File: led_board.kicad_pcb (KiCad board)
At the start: 2 copper layers, 12 parts, among them J1 Conn_Coaxial, J2 Conn_Coaxial, J3 Conn_Coaxial, J4 Conn_Coaxial

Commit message: edits
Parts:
- moved D4 124.5 mm to (52.5, 109.7), turned to 270 degrees
- moved R4 121.5 mm to (49.2, 109.7)
- moved R3 114.5 mm to (49.0, 87.4)
- moved J4 112.4 mm to (40.4, 109.7), turned to 180 degrees
- moved D3 6.88 mm to (53.2, 88.8), turned to 0 degrees
- moved D2 0.76 mm to (53.0, 65.0)
- moved J2 0.76 mm to (40.4, 65.0)
- moved R2 0.76 mm to (47.6, 65.0)
- moved J3 0.72 mm to (40.4, 87.4)
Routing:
- net Net-(D3-Pad2): track 0.00 -> 29.8 mm
- net Net-(D4-Pad2): track 0.00 -> 29.8 mm
- net Net-(J4-Pad1): track 0.00 -> 7.90 mm
- net Net-(J3-Pad1): track 0.00 -> 7.77 mm
- net Net-(D3-Pad1): track 0.00 -> 3.00 mm
- net Net-(D4-Pad1): track 0.00 -> 2.86 mm

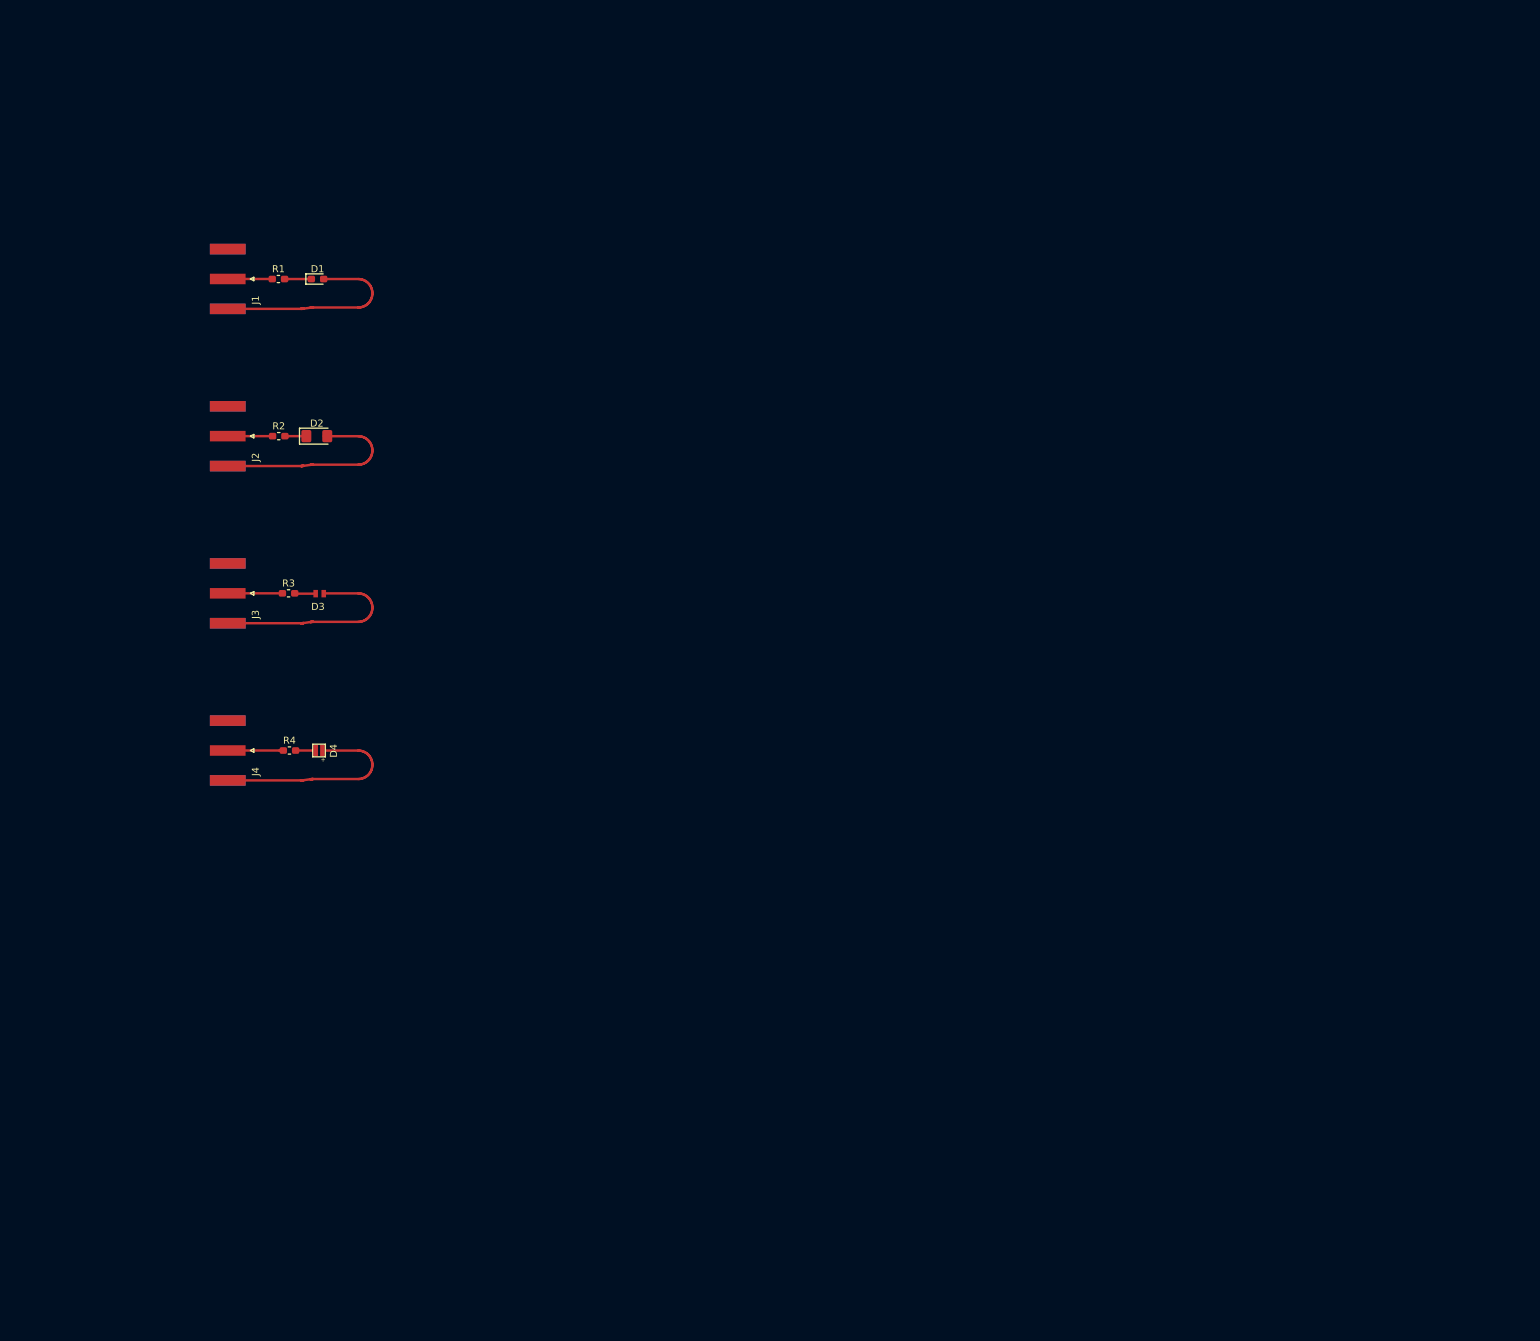
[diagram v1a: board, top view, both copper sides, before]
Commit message: rework for thorlabs 30mm cage
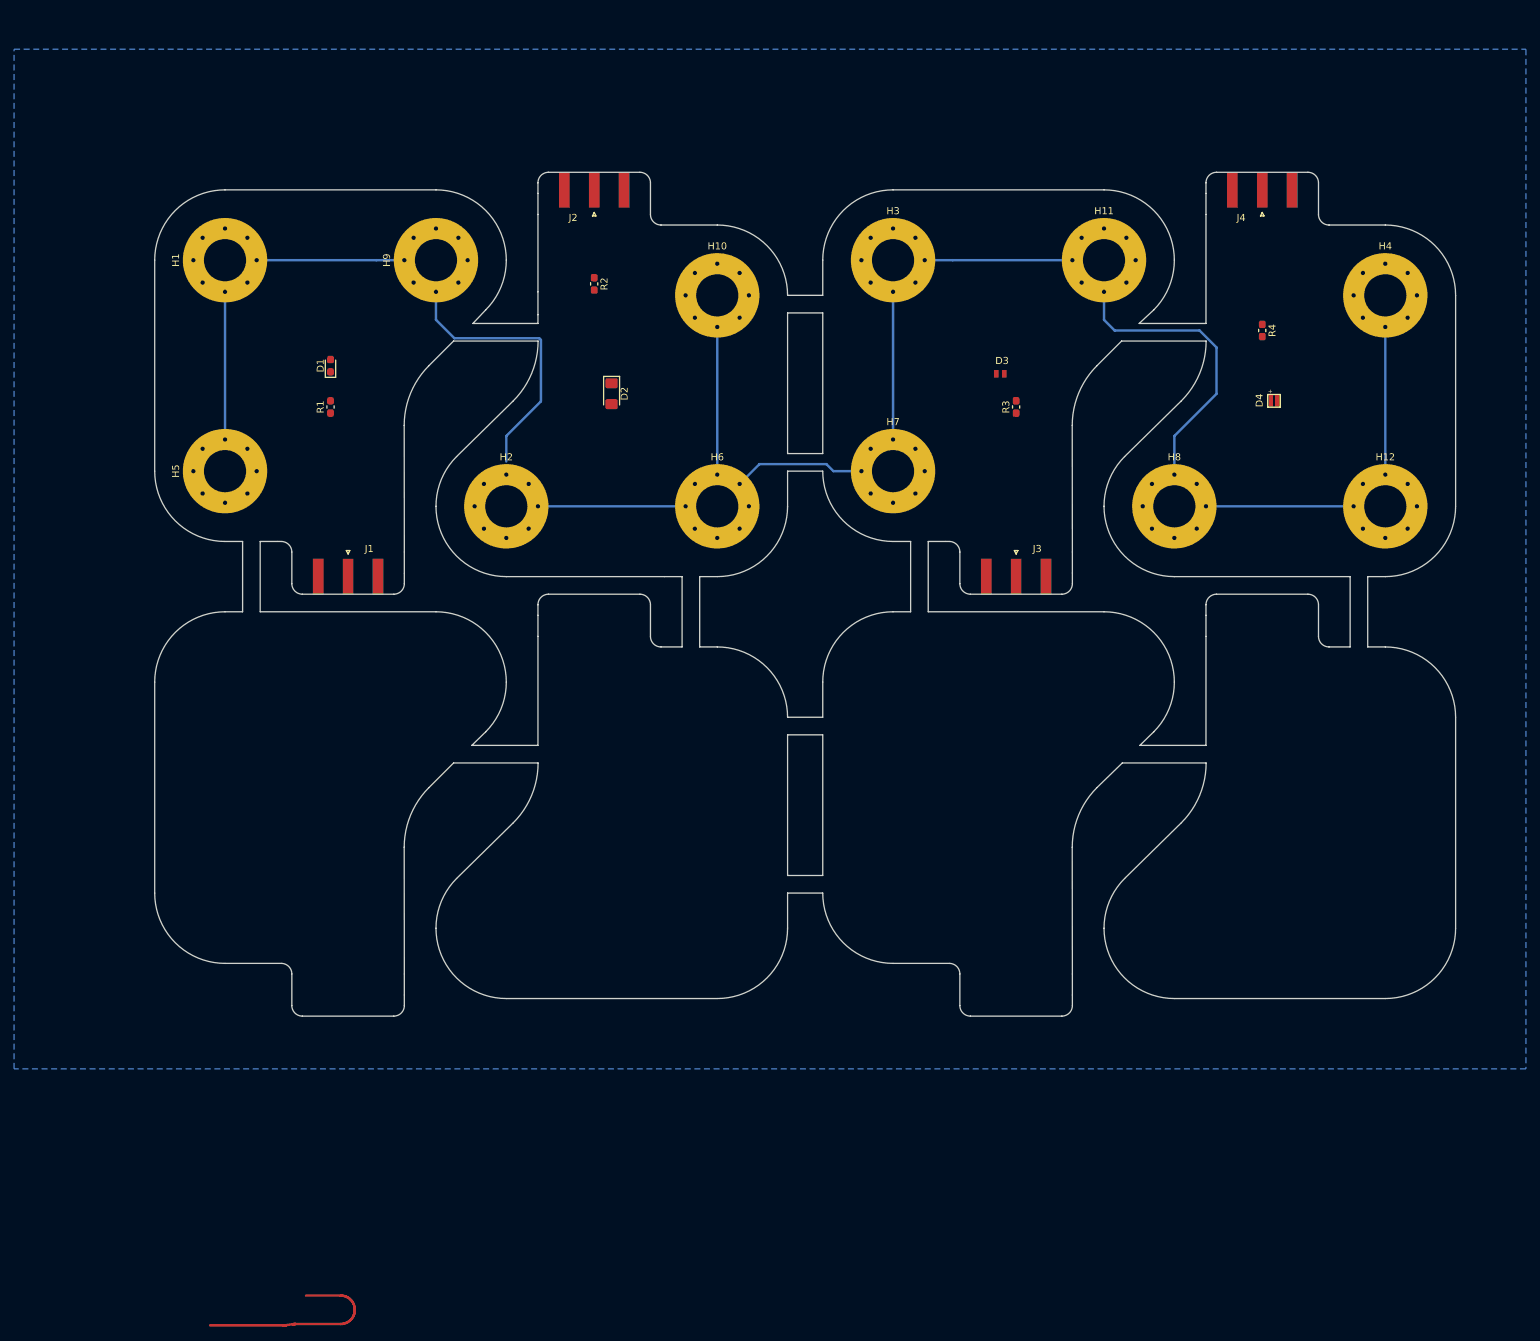
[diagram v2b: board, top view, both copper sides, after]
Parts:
- added H1: MountingHole_Pad, MountingHole:MountingHole_6mm_Pad_Via, F.Cu at (40.0, 40.0)
- added H10: MountingHole_Pad, MountingHole:MountingHole_6mm_Pad_Via, F.Cu at (110.0, 45.0)
- added H11: MountingHole_Pad, MountingHole:MountingHole_6mm_Pad_Via, F.Cu at (165.0, 40.0)
- added H12: MountingHole_Pad, MountingHole:MountingHole_6mm_Pad_Via, F.Cu at (205.0, 75.0)
- added H2: MountingHole_Pad, MountingHole:MountingHole_6mm_Pad_Via, F.Cu at (80.0, 75.0)
- added H3: MountingHole_Pad, MountingHole:MountingHole_6mm_Pad_Via, F.Cu at (135.0, 40.0)
- added H4: MountingHole_Pad, MountingHole:MountingHole_6mm_Pad_Via, F.Cu at (205.0, 45.0)
- added H5: MountingHole_Pad, MountingHole:MountingHole_6mm_Pad_Via, F.Cu at (40.0, 70.0)
- added H6: MountingHole_Pad, MountingHole:MountingHole_6mm_Pad_Via, F.Cu at (110.0, 75.0)
- added H7: MountingHole_Pad, MountingHole:MountingHole_6mm_Pad_Via, F.Cu at (135.0, 70.0)
- added H8: MountingHole_Pad, MountingHole:MountingHole_6mm_Pad_Via, F.Cu at (175.0, 75.0)
- added H9: MountingHole_Pad, MountingHole:MountingHole_6mm_Pad_Via, F.Cu at (70.0, 40.0)
- moved J4 167.3 mm to (187.5, 30.0), turned to 90 degrees
- moved R4 150.7 mm to (187.5, 50.0), turned to 270 degrees
- moved D4 146.2 mm to (190.0, 60.0), turned to 90 degrees
- moved J3 112.1 mm to (152.5, 85.0), turned to 270 degrees
- moved R3 106.8 mm to (152.5, 60.9), turned to 90 degrees
- moved D3 103.0 mm to (150.5, 54.8), turned to 180 degrees
- moved J2 62.8 mm to (92.5, 30.0), turned to 90 degrees
- moved R2 49.8 mm to (92.5, 43.4), turned to 270 degrees
- moved J1 45.7 mm to (57.5, 85.0), turned to 270 degrees
- moved D2 42.4 mm to (95.0, 59.0), turned to 270 degrees
- moved R1 19.6 mm to (55.0, 60.9), turned to 90 degrees
- moved D1 12.5 mm to (55.0, 55.0), turned to 90 degrees
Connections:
- D1 pad 1: Net-(D1-Pad1) -> (no net)
- D1 pad 2: Net-(D1-Pad2) -> (no net)
- J1 pad 1: Net-(J1-Pad1) -> (no net)
- J1 pad 2: Net-(D1-Pad2) -> (no net)
- R1 pad 1: Net-(J1-Pad1) -> (no net)
- R1 pad 2: Net-(D1-Pad1) -> (no net)
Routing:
- net GND: track 0.00 -> 363.0 mm
- net Net-(D1-Pad2): track 29.8 -> 0.00 mm
- net Net-(D3-Pad2): track 29.8 -> 0.00 mm
- net Net-(D2-Pad2): track 29.8 -> 0.00 mm
- net Net-(J4-Pad1): track 7.90 -> 0.00 mm
- net Net-(J3-Pad1): track 7.77 -> 0.00 mm
- net Net-(J1-Pad1): track 6.32 -> 0.00 mm
- net Net-(J2-Pad1): track 6.32 -> 0.00 mm
- net Net-(D1-Pad1): track 3.81 -> 0.00 mm
- net Net-(D2-Pad1): track 3.57 -> 0.00 mm
- net Net-(D3-Pad1): track 3.00 -> 0.00 mm
- net Net-(D4-Pad1): track 2.86 -> 0.00 mm
- added copper zone on B.Cu, net GND
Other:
- board outline added: 185 x 120 mm
- board text added: "£135 for board 2 layer PTH FR4 1oz Cu Au/Ni 0.8mm"

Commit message: fcu pour
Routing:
- added copper zone on F.Cu, net GND
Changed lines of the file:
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@@
   )
   (setup
-    (last_trace_width 0.349)
+    (last_trace_width 0.25)
     (user_trace_width 0.349)
     (trace_clearance 0.2)
@@
   (gr_line (start 65.479186 63.5) (end 65.5 81.5) (layer Edge.Cuts) (width 0.05))
   (gr_arc (start 48 81.5) (end 49.5 81.5) (angle -90) (layer Edge.Cuts) (width 0.05))
-  (segment (start 61.514719 40) (end 40 40) (width 0.349) (layer B.Cu) (net 10))
-  (segment (start 70 40) (end 61.514719 40) (width 0.349) (layer B.Cu) (net 10))
-  (segment (start 40 40) (end 40 70) (width 0.349) (layer B.Cu) (net 10))
-  (segment (start 84.921817 51.333897) (end 84.921817 60.078183) (width 0.349) (layer B.Cu) (net 10))
-  (segment (start 84.68841 51.10049) (end 84.921817 51.333897) (width 0.349) (layer B.Cu) (net 10))
-  (segment (start 72.615209 51.10049) (end 84.68841 51.10049) (width 0.349) (layer B.Cu) (net 10))
-  (segment (start 70 40) (end 70 48.485281) (width 0.349) (layer B.Cu) (net 10))
-  (segment (start 70 48.485281) (end 72.615209 51.10049) (width 0.349) (layer B.Cu) (net 10))
-  (segment (start 84.921817 60.078183) (end 80 65) (width 0.349) (layer B.Cu) (net 10))
-  (segment (start 80 65) (end 80 68.625499) (width 0.349) (layer B.Cu) (net 10))
   (segment (start 48.584912 191.461938) (end 48.609713 191.459153) (width 0.349) (layer F.Cu) (net 5))
   (segment (start 48.609713 191.459153) (end 48.634488 191.456146) (width 0.349) (layer F.Cu) (net 5))
@@
   (segment (start 57.217366 191.131759) (end 57.394793 191.047842) (width 0.349) (layer F.Cu) (net 5))
   (segment (start 58.41357 189.67418) (end 58.442369 189.480034) (width 0.349) (layer F.Cu) (net 5))
+  (segment (start 61.514719 40) (end 40 40) (width 0.349) (layer B.Cu) (net 10))
+  (segment (start 70 40) (end 61.514719 40) (width 0.349) (layer B.Cu) (net 10))
+  (segment (start 40 40) (end 40 70) (width 0.349) (layer B.Cu) (net 10))
+  (segment (start 84.921817 51.333897) (end 84.921817 60.078183) (width 0.349) (layer B.Cu) (net 10))
+  (segment (start 84.68841 51.10049) (end 84.921817 51.333897) (width 0.349) (layer B.Cu) (net 10))
+  (segment (start 72.615209 51.10049) (end 84.68841 51.10049) (width 0.349) (layer B.Cu) (net 10))
+  (segment (start 70 40) (end 70 48.485281) (width 0.349) (layer B.Cu) (net 10))
+  (segment (start 70 48.485281) (end 72.615209 51.10049) (width 0.349) (layer B.Cu) (net 10))
+  (segment (start 84.921817 60.078183) (end 80 65) (width 0.349) (layer B.Cu) (net 10))
+  (segment (start 80 65) (end 80 68.625499) (width 0.349) (layer B.Cu) (net 10))
   (segment (start 80 75) (end 110 75) (width 0.349) (layer B.Cu) (net 10))
   (segment (start 110 75) (end 110 45) (width 0.349) (layer B.Cu) (net 10))
@@
       )
     )
+  )
+  (zone (net 10) (net_name GND) (layer F.Cu) (hatch edge 0.508)
+    (connect_pads (clearance 0.508))
+    (min_thickness 0.254)
+    (fill yes (arc_segments 32) (thermal_gap 0.508) (thermal_bridge_width 0.508))
+    (polygon
+      (pts
+        (xy 225 155) (xy 14 155) (xy 14 5) (xy 225 5)
+      )
+    )

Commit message: no res term boards added, net class updated
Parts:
- added D5: 405LED1, LED_SMD:LED_0603_1608Metric_Pad1.05x0.95mm_HandSolder, F.Cu at (55.0, 115.0)
- added D6: 405LED2, LED_SMD:LED_1206_3216Metric_Pad1.42x1.75mm_HandSolder, F.Cu at (95.0, 120.0)
- added D7: 375LED1, leds:LED_SMD_Kingbright_405_2012, F.Cu at (150.2, 113.8)
- added D8: 375LED2, leds:LED_SMD_Vishay_405_16, F.Cu at (189.2, 120.0)
- added H13: MountingHole_Pad, MountingHole:MountingHole_6mm_Pad_Via, F.Cu at (40.0, 130.0)
- added H14: MountingHole_Pad, MountingHole:MountingHole_6mm_Pad_Via, F.Cu at (110.0, 105.0)
- added H15: MountingHole_Pad, MountingHole:MountingHole_6mm_Pad_Via, F.Cu at (135.0, 100.0)
- added H16: MountingHole_Pad, MountingHole:MountingHole_6mm_Pad_Via, F.Cu at (205.0, 105.0)
- added H17: MountingHole_Pad, MountingHole:MountingHole_6mm_Pad_Via, F.Cu at (40.0, 100.0)
- added H18: MountingHole_Pad, MountingHole:MountingHole_6mm_Pad_Via, F.Cu at (80.0, 135.0)
- added H19: MountingHole_Pad, MountingHole:MountingHole_6mm_Pad_Via, F.Cu at (165.0, 100.0)
- added H20: MountingHole_Pad, MountingHole:MountingHole_6mm_Pad_Via, F.Cu at (175.0, 135.0)
- added H21: MountingHole_Pad, MountingHole:MountingHole_6mm_Pad_Via, F.Cu at (70.0, 100.0)
- added H22: MountingHole_Pad, MountingHole:MountingHole_6mm_Pad_Via, F.Cu at (110.0, 135.0)
- added H23: MountingHole_Pad, MountingHole:MountingHole_6mm_Pad_Via, F.Cu at (135.0, 130.0)
- added H24: MountingHole_Pad, MountingHole:MountingHole_6mm_Pad_Via, F.Cu at (205.0, 135.0)
- added J5: Conn_Coaxial, Connector_Coaxial:SMA_Amphenol_132289_EdgeMount, F.Cu at (57.5, 145.0)
- added J6: Conn_Coaxial, Connector_Coaxial:SMA_Amphenol_132289_EdgeMount, F.Cu at (92.5, 90.0)
- added J7: Conn_Coaxial, Connector_Coaxial:SMA_Amphenol_132289_EdgeMount, F.Cu at (152.5, 145.0)
- added J8: Conn_Coaxial, Connector_Coaxial:SMA_Amphenol_132289_EdgeMount, F.Cu at (187.5, 90.0)
- moved R2 12.8 mm to (96.5, 55.5)
- moved R4 7.05 mm to (190.5, 56.4)
- moved R3 3.83 mm to (149.5, 58.5)
- moved D3 1.76 mm to (149.7, 56.4), turned to 0 degrees
- moved D2 1.01 mm to (95.0, 60.0), turned to 180 degrees
- moved D4 1.00 mm to (191.0, 60.0)
- moved R1 0.12 mm to (55.0, 61.0)
- turned D1 to 0 degrees
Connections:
- D1 pad 1: (no net) -> Net-(D1-Pad1)
- D1 pad 2: (no net) -> Net-(D1-Pad2)
- J1 pad 1: (no net) -> Net-(J1-Pad1)
- J1 pad 2: (no net) -> Net-(D1-Pad2)
- R1 pad 1: (no net) -> Net-(J1-Pad1)
- R1 pad 2: (no net) -> Net-(D1-Pad1)
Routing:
- net Net-(D1-Pad2): track 0.00 -> 33.7 mm
- net Net-(D4-Pad2): track 29.8 -> 0.00 mm
- net Net-(J1-Pad1): track 0.00 -> 24.2 mm
- net Net-(D1-Pad1): track 0.00 -> 5.49 mm
- net Net-(D5-Pad2): track 0.00 -> 0.52 mm
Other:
- net class RFLine added: clearance 2, trace_width 1.51, via_dia 0.8, via_drill 0.4
- board text added: "30mm"
- board text added: "375nm"
- board text added: "405nm"
- board text added: "Dsg: W Matthews Chk: G Faulkner"
- board text added: "LED TX Board Vishay 0603 XX-XX-XX DK"
- board text added: "TODO: Add Digikey Part No for each part"

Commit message: Fixed a big dumb. nearly done.
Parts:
- added REF**: uv_warn, warnings:uv_warn, B.Cu at (45.0, 110.0)
- added REF**: uv_warn, warnings:uv_warn, B.Cu at (105.0, 125.0)
- added REF**: uv_warn, warnings:uv_warn, B.Cu at (140.0, 110.0)
- added REF**: uv_warn, warnings:uv_warn, B.Cu at (200.0, 125.0)
- added REF**: uv_warn, warnings:uv_warn, B.Cu at (200.0, 65.0)
- added REF**: uv_warn, warnings:uv_warn, B.Cu at (140.0, 50.0)
- added REF**: uv_warn, warnings:uv_warn, B.Cu at (105.0, 65.0)
- added REF**: uv_warn, warnings:uv_warn, B.Cu at (45.0, 50.0)
- moved R1 5.16 mm to (52.1, 56.8)
- moved R4 3.62 mm to (193.0, 59.0)
- moved R3 2.55 mm to (147.0, 58.0)
- turned D5 to 0 degrees
- turned D6 to 180 degrees
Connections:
- D5 pad 1: Net-(D5-Pad1) -> GND
- D6 pad 1: Net-(D6-Pad1) -> GND
- D7 pad 1: Net-(D7-Pad1) -> GND
- D8 pad 1: Net-(D8-Pad1) -> GND
- J1 pad 1: Net-(J1-Pad1) -> Net-(D1-Pad2)
- J1 pad 2: Net-(D1-Pad2) -> GND
- J2 pad 1: Net-(J2-Pad1) -> Net-(D2-Pad2)
- J2 pad 2: Net-(D2-Pad2) -> GND
- J3 pad 1: Net-(J3-Pad1) -> Net-(D3-Pad2)
- J3 pad 2: Net-(D3-Pad2) -> GND
- J4 pad 1: Net-(J4-Pad1) -> Net-(D4-Pad2)
- J4 pad 2: Net-(D4-Pad2) -> GND
- J5 pad 1: Net-(D5-Pad1) -> Net-(D5-Pad2)
- J5 pad 2: Net-(D5-Pad2) -> GND
- J6 pad 1: Net-(D6-Pad1) -> Net-(D6-Pad2)
- J6 pad 2: Net-(D6-Pad2) -> GND
- J7 pad 1: Net-(D7-Pad1) -> Net-(D7-Pad2)
- J7 pad 2: Net-(D7-Pad2) -> GND
- J8 pad 1: Net-(D8-Pad1) -> Net-(D8-Pad2)
- J8 pad 2: Net-(D8-Pad2) -> GND
- R1 pad 1: Net-(J1-Pad1) -> GND
- R2 pad 1: Net-(J2-Pad1) -> GND
- R3 pad 1: Net-(J3-Pad1) -> GND
- R4 pad 1: Net-(J4-Pad1) -> GND
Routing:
- net GND: track 363.0 -> 421.4 mm, vias 0 -> 51
- net Net-(D7-Pad2): track 0.00 -> 30.4 mm
- net Net-(D8-Pad2): track 0.00 -> 30.4 mm
- net Net-(D3-Pad2): track 0.00 -> 30.1 mm
- net Net-(D4-Pad2): track 0.00 -> 30.1 mm
- net Net-(D2-Pad2): track 0.00 -> 30.0 mm
- net Net-(D6-Pad2): track 0.00 -> 30.0 mm
- net Net-(D5-Pad2): track 0.52 -> 29.8 mm
- net Net-(J1-Pad1): track 24.2 -> 0.00 mm
- net Net-(D2-Pad1): track 0.00 -> 3.63 mm
- net Net-(D1-Pad2): track 33.7 -> 30.1 mm
- net Net-(D1-Pad1): track 5.49 -> 2.24 mm
- net Net-(D3-Pad1): track 0.00 -> 2.92 mm
- net Net-(D4-Pad1): track 0.00 -> 2.00 mm
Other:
- net class RFLine: clearance 2 -> 1.5
